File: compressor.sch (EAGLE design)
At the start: 38 parts, among them X1 OPAMP, X2 OPAMP, X3 OPAMP, X4 OPAMP, X5 OPAMP, X6 OPAMP, X7 OPAMP, X8 OPAMP

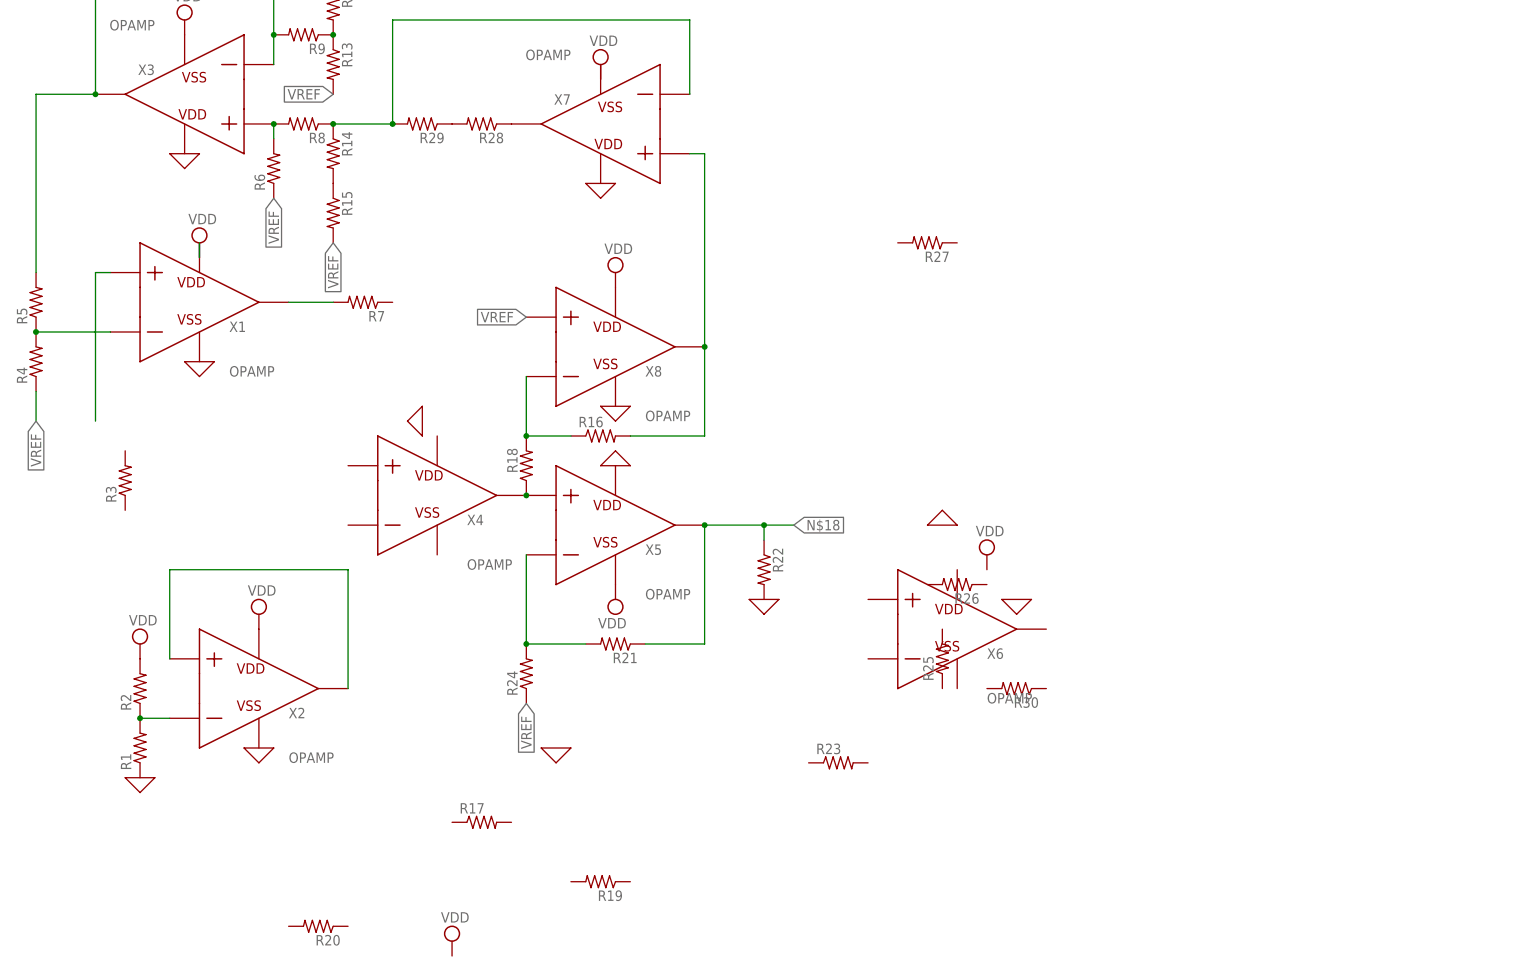
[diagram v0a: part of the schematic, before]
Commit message: Update compressor schematic
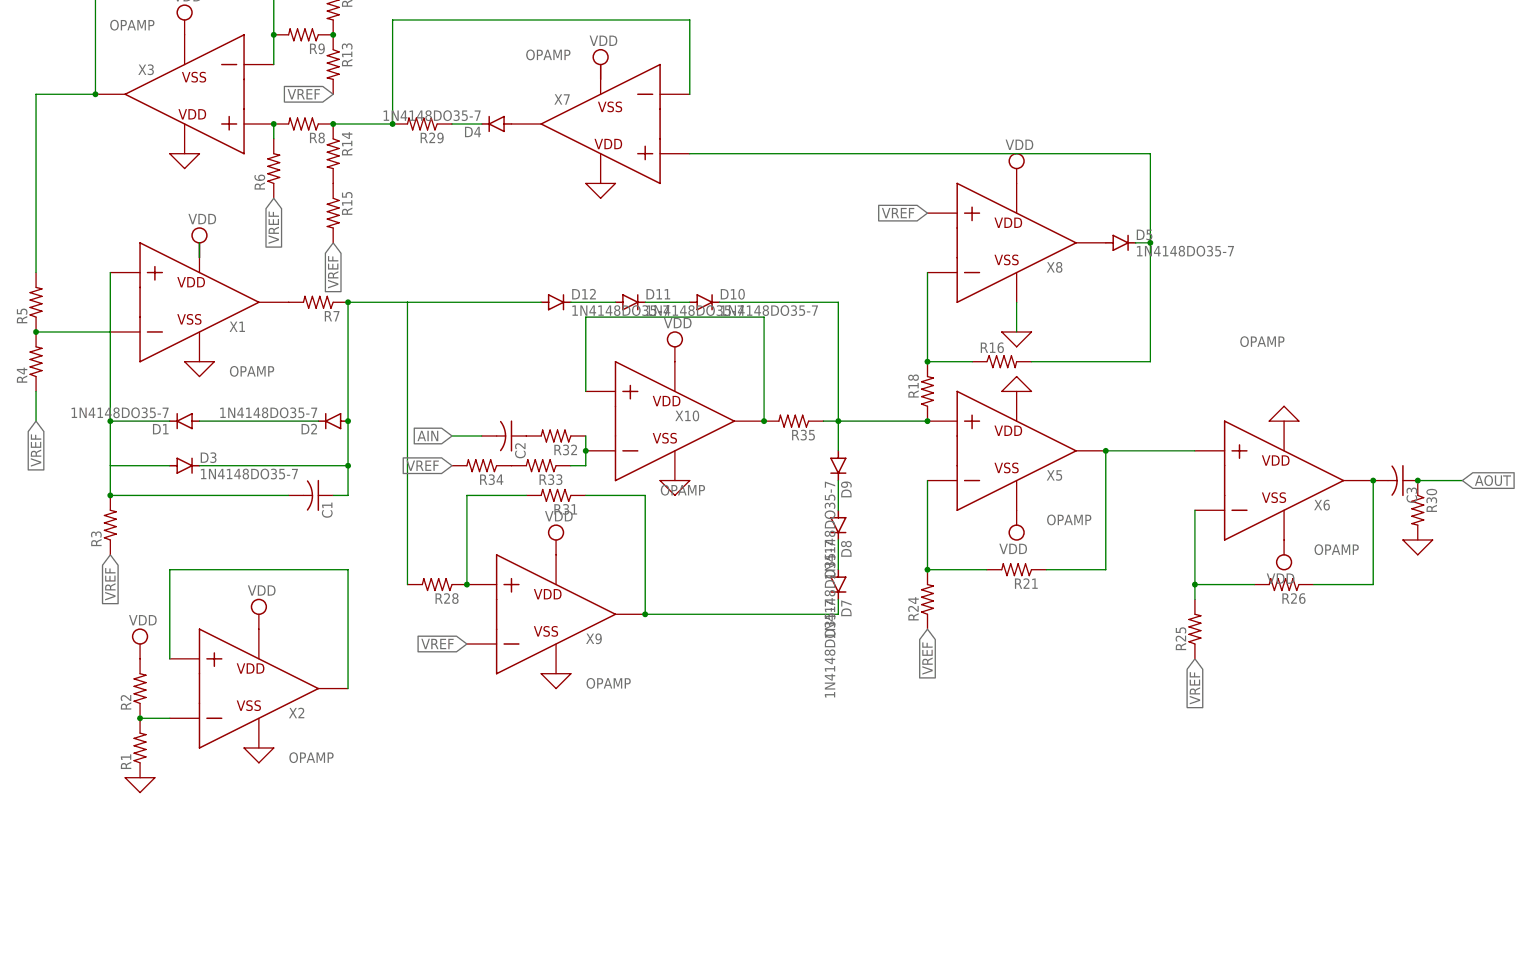
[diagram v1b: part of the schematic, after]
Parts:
- removed R17, R19, R20, R22, R23, R27: (no value), rcl:R-US_0204/7
- removed X4: OPAMP, ngspice-simulation:OPAMP
- added C1, C2, C3: (no value), rcl:C-US025-024X044
- added D1, D10, D11, D12, D2, D3, D4, D5, D7, D8, D9: 1N4148DO35-7, diode:1N4148DO35-7
- added R31, R32, R33, R34, R35: (no value), rcl:R-US_0204/7
- added X10, X9: OPAMP, ngspice-simulation:OPAMP
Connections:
- removed net N$17: R18.1, X4.VOUT, X5.P
- new net AIN: C2.2
- new net AOUT: C3.1, R30.1
- new net N$20: D1.A, D2.C
- new net N$21: C1.1, D12.A, D2.A, D3.C, R28.2, R7.1
- new net N$22: R28.1, R31.2, X9.P
- new net N$23: D7.C, R31.1, X9.VOUT
- new net N$24: D8.A, D9.C
- new net N$25: D7.A, D8.C
- new net N$26: D10.C, D9.A, R18.1, R35.1, X5.P
- new net N$27: R35.2, X10.P, X10.VOUT
- new net N$28: R33.2, R34.1
- new net N$29: R32.1, R33.1, X10.N
- new net N$30: C2.1, R32.2
- new net N$31: D11.A, D12.C
- new net N$32: D10.A, D11.C
- new net N$33: D5.A, X8.VOUT
- new net N$34: C3.2, R26.1, X6.VOUT
- new net N$35: R25.2, R26.2, X6.N
- net 0: now also R30.2, X10.VSS, X6.VDD, X9.VSS; no longer R22.2
- net N$13: now also D4.C; no longer R28.2
- net N$14: now also D4.A; no longer R28.1
- net N$15: now also D5.C; no longer X8.VOUT
- net N$18: now also X6.P; no longer R22.1
- net N$3: now also C1.2, D1.C, D3.A, R3.2
- net VDD: now also X10.VDD, X6.VSS, X9.VDD
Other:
- moved on the sheet: R16, R18, R21, R24, R25, R26, R28, R3, R30, R7, X5, X6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

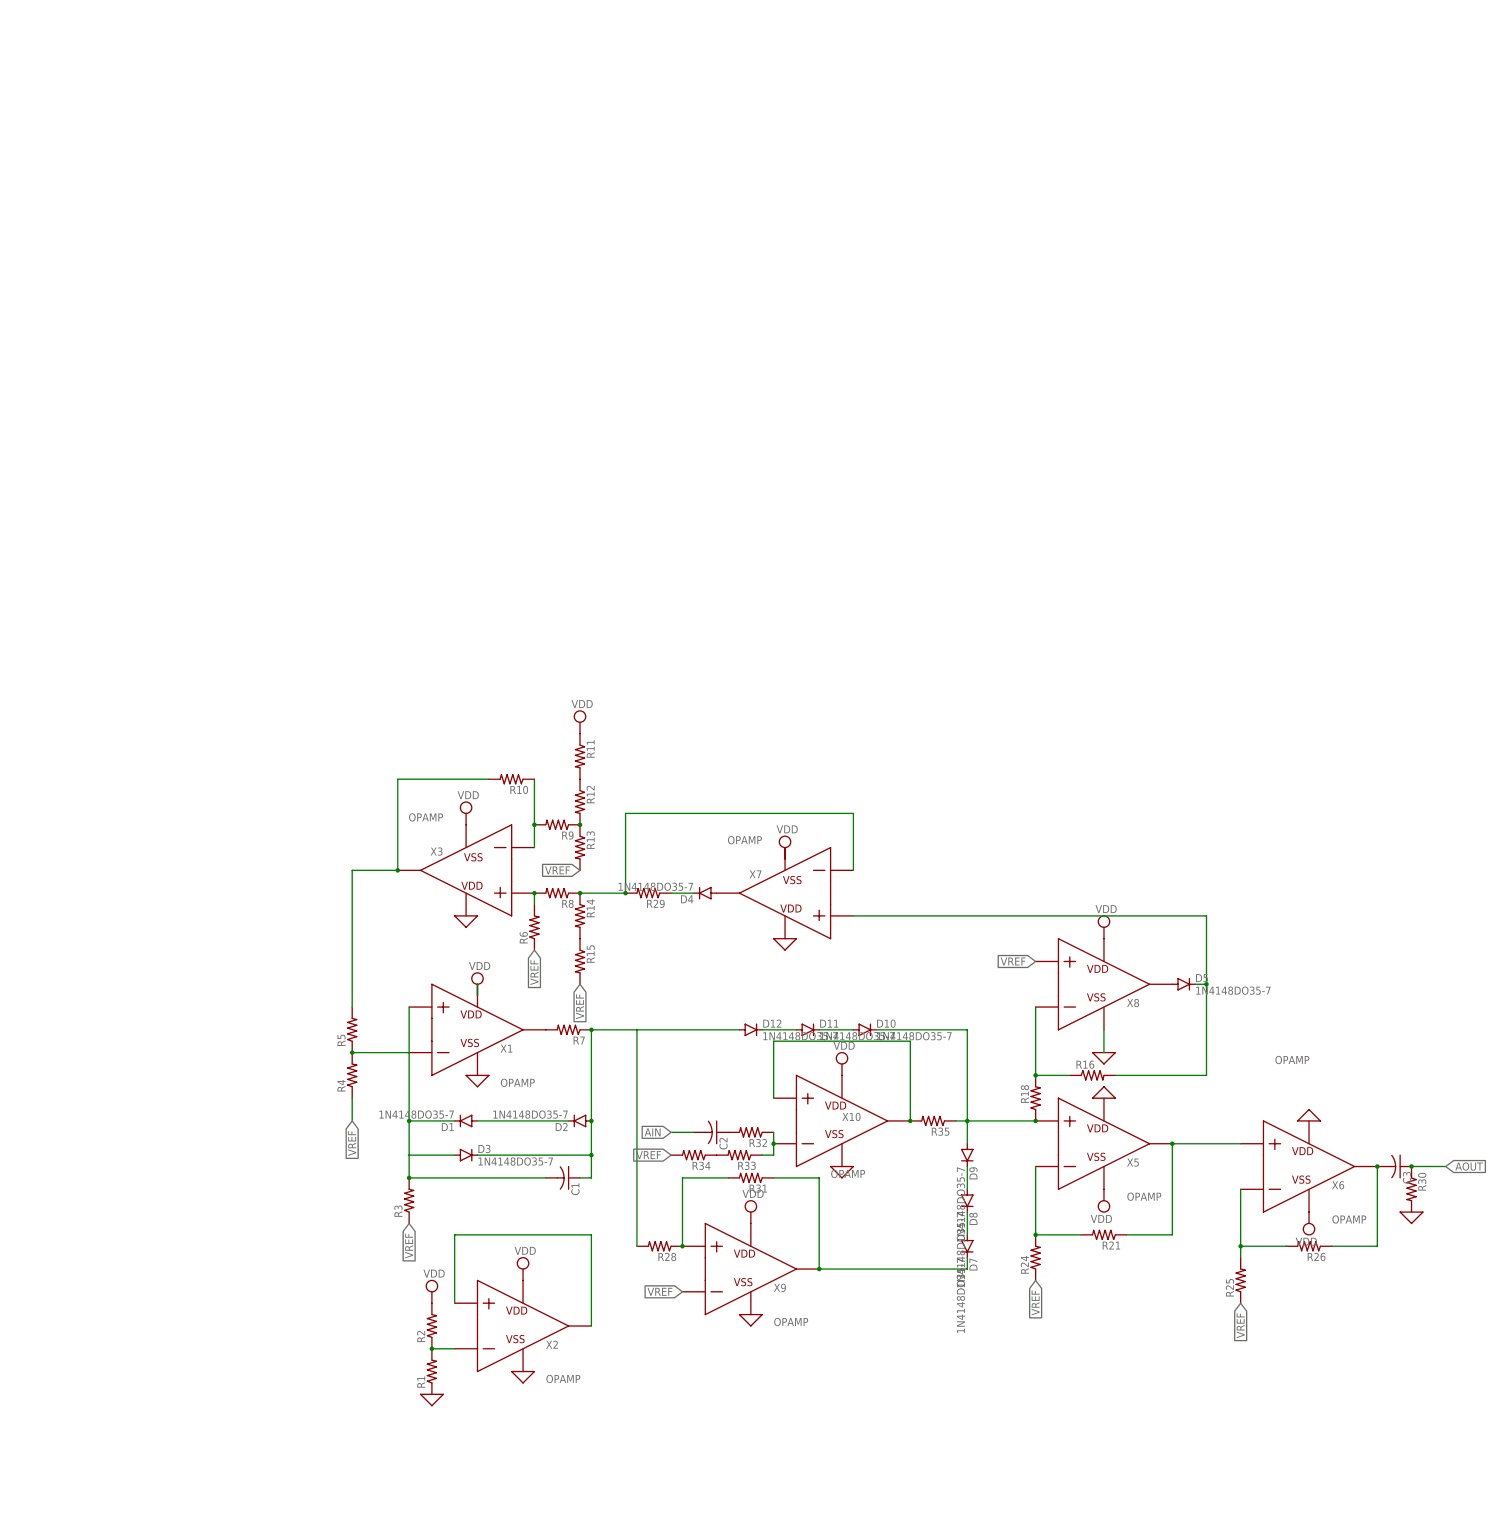
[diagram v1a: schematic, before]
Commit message: update compressor with digital pots Added to man schem with muxes
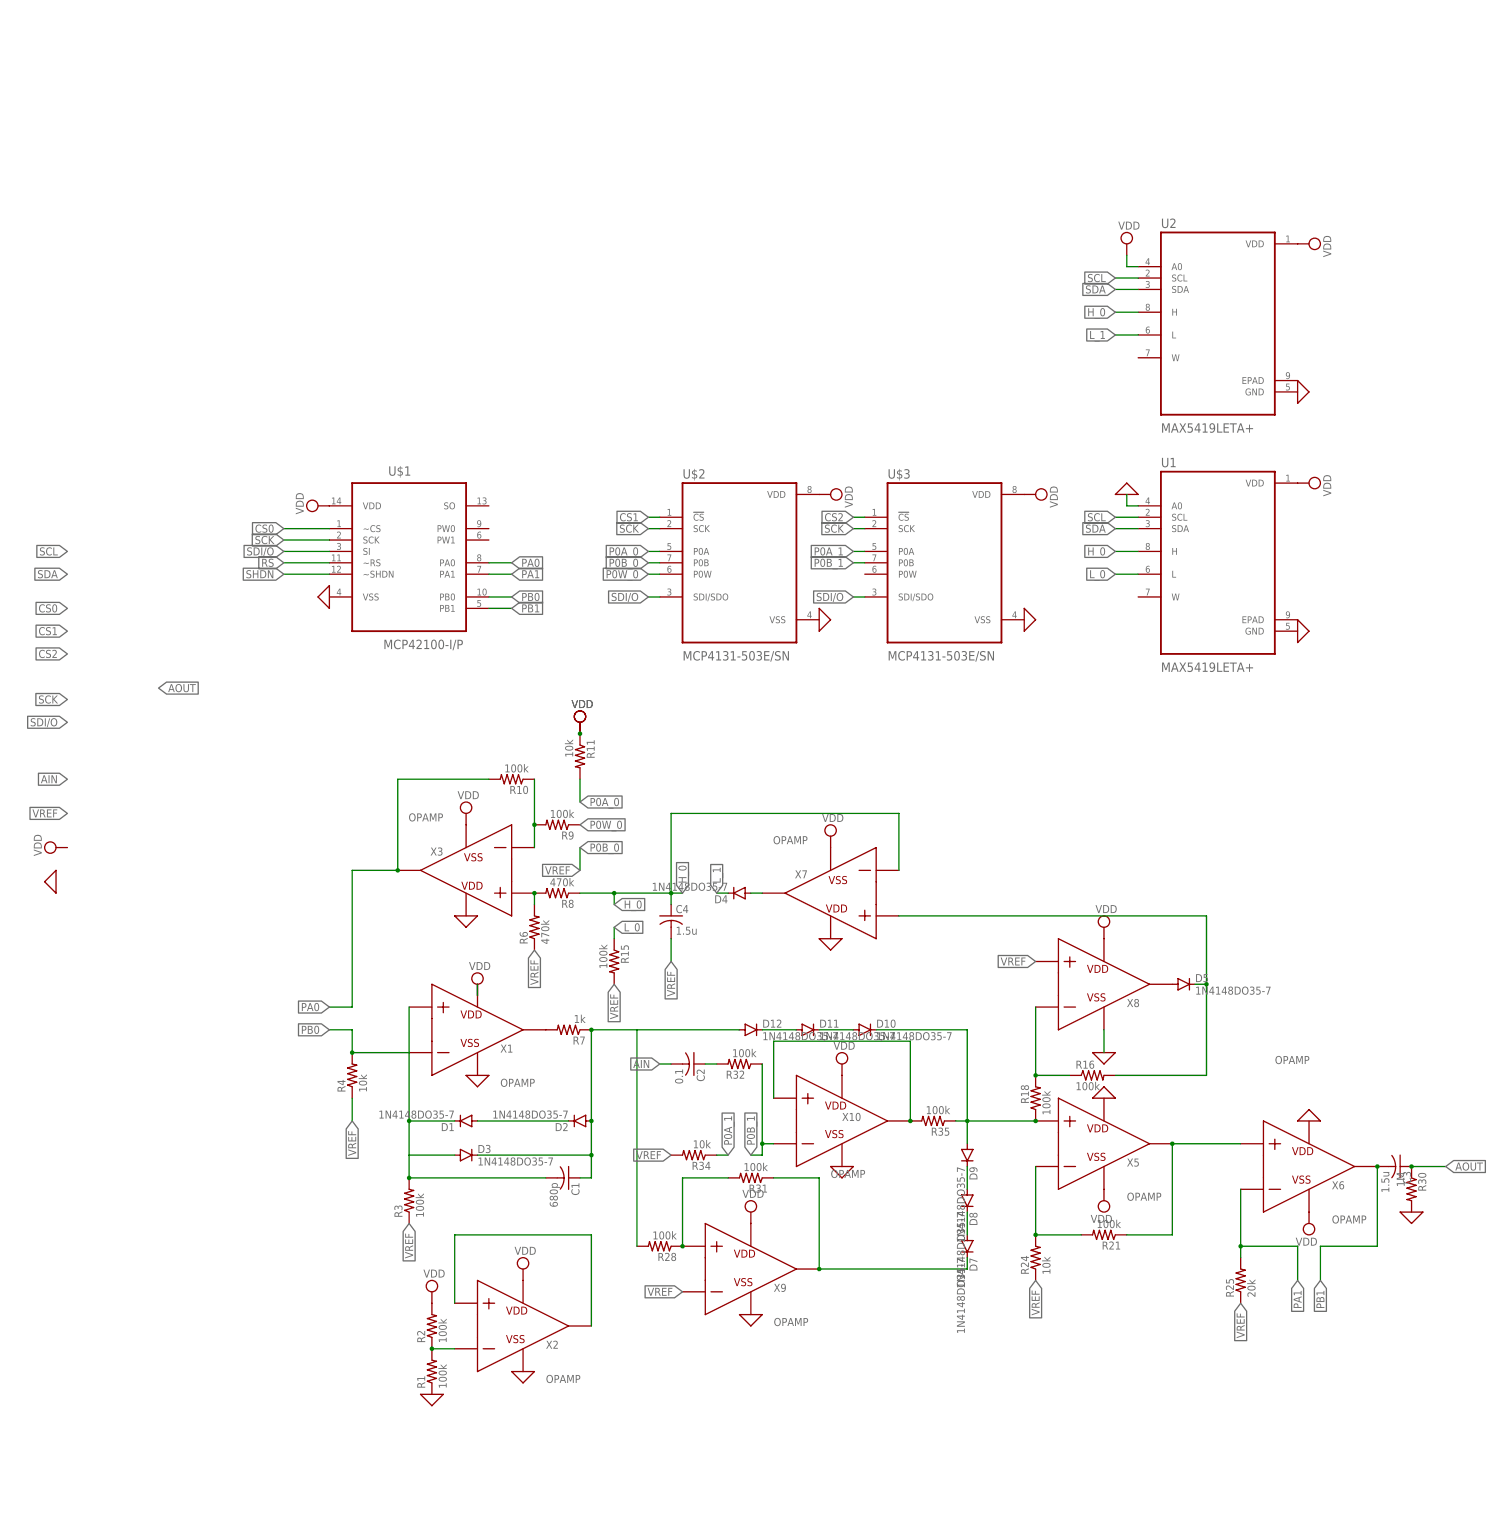
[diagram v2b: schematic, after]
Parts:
- removed R12, R13, R14, R26, R29, R33, R5: (no value), rcl:R-US_0204/7
- added C4: 1.5u, rcl:C-US025-024X044
- added U$1: MCP42100-I/P, MCP42100-I_P:MCP42100-I/P
- added U$2, U$3: MCP4131-503E/SN, MCP4131-503E_SN:MCP4131-503E/SN
- added U1, U2: MAX5419LETA+, MAX5419LETA_:MAX5419LETA+
- C1: value (none) -> 680p
- C2: value (none) -> 0.1
- C3: value (none) -> 1.5u
- R1, R10, R15, R16, R18, R2, R21, R28, R3, R31, R32, R35, R9: value (none) -> 100k
- R11, R24, R34, R4: value (none) -> 10k
- R25: value (none) -> 20k
- R30: value (none) -> 1M
- R6, R8: value (none) -> 470k
- R7: value (none) -> 1k
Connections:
- removed net N$12: R14.2, R15.1
- removed net N$13: D4.C, R29.1
- removed net N$2: R4.2, R5.1, X1.N
- removed net N$28: R33.2, R34.1
- removed net N$29: R32.1, R33.1, X10.N
- removed net N$34: C3.2, R26.1, X6.VOUT
- removed net N$35: R25.2, R26.2, X6.N
- removed net N$8: R10.2, R5.2, X3.VOUT
- removed net N$9: R12.2, R13.1, R9.1
- new net CS0: U$1.~CS
- new net CS1: U$2.!CS
- new net CS2: U$3.!CS
- new net H_0: C4.1, R8.1, U1.H, U2.H, X7.N
- new net L_0: R15.1, U1.L
- new net L_1: D4.C, U2.L
- new net P0A_0: U$2.P0A
- new net P0A_1: R34.1, U$3.P0A
- new net P0B_0: U$2.P0B
- new net P0B_1: R32.1, U$3.P0B, X10.N
- new net P0W_0: U$2.P0W
- new net PA0: R10.2, U$1.PA0, X3.VOUT
- new net PA1: R25.2, U$1.PA1, X6.N
- new net PB0: R4.2, U$1.PB0, X1.N
- new net PB1: C3.2, U$1.PB1, X6.VOUT
- new net RS: U$1.~RS
- new net SCK: U$1.SCK, U$2.SCK, U$3.SCK
- new net SCL: U1.SCL, U2.SCL
- new net SDA: U1.SDA, U2.SDA
- new net SDI/O: U$1.SI, U$2.SDI/SDO, U$3.SDI/SDO
- new net SHDN: U$1.~SHDN
- net 0: now also U$1.VSS, U$2.VSS, U$3.VSS, U1.A0, U1.GND, U2.GND
- net N$10: no longer R12.1
- net N$11: now also C4.2; no longer R14.1, R29.2, R8.1, X7.N
- net VDD: now also U$1.VDD, U$2.VDD, U$3.VDD, U1.VDD, U2.A0, U2.VDD, X7.VSS
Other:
- moved on the sheet: C2, D4, R15, R32, X7
